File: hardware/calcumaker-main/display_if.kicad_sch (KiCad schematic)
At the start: 10 parts, among them J3 TO DISPLAY, U5 TPS61022RWUR, U6 74HCT125

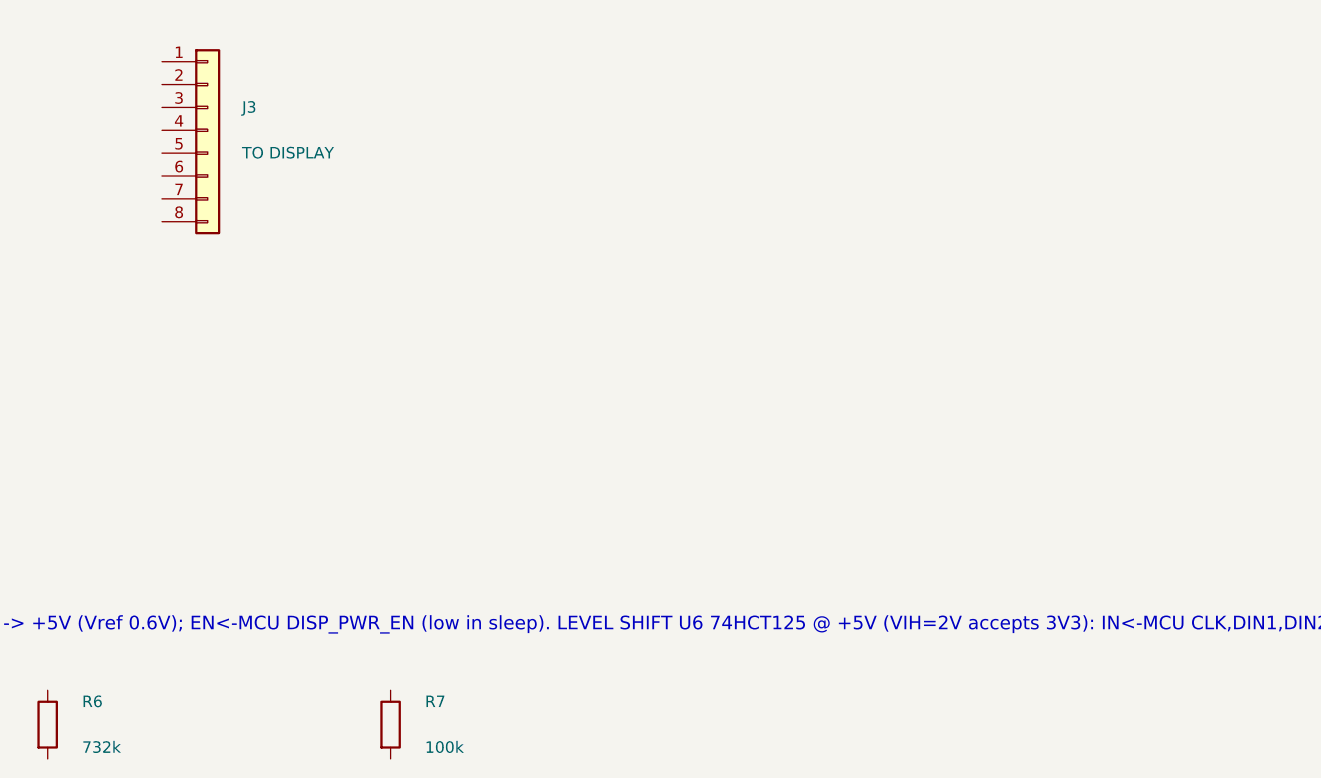
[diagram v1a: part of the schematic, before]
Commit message: Error handling: HP-style glass codes + DNP-optional aux OLED (display board)
Two layers, per design discussion:

ENGINE/APP — CalcError restructured: TypeError(&str) becomes Op(code, msg)
with class constructors at every site; code() gives the HP-16C-style glass
class (0 math domain, 1 register/flag, 2 bits/shift/word, 3 mode ranges,
4 too large, 5 no solution, 6 stack/entry, 7 dates, 8 statistics, 9 reserved
for crash recovery), text() the full string. App shows a transient 'Error N'
on the X row (cleared by the next key, like SHOW) and keeps the full text on
the status line — the duplicated error-string mapping in run_owned/flush is
now one report() helper. All of 'Error N' renders on the 7-seg. 211 tests.

HARDWARE — the aux OLED lands on the DISPLAY board (user decision): new
AuxDisplay sheet with J2, a 1x4 socket (PZ254V-11-04P C2691448) receiving a
standard 0.91in SSD1306 128x32 I2C module, DNP by default, hand-placed with
the THT digits. Interconnect grows 1x8 -> 1x10 (PZ254V-11-10P C492409, both
boards, pinout now ... 8=+3V3 9=SDA 10=SCL); I2C pull-ups R14/R15 4.7k on
the main board, DNP with the OLED. Both boards regenerate + check clean
(main 161, display 22 components). DESIGN.md documents the layered error
story and names the reusable 'DNP-optional aux' pattern; PARTS.md updated.

Co-Authored-By: Claude Fable 5 <noreply@anthropic.com>
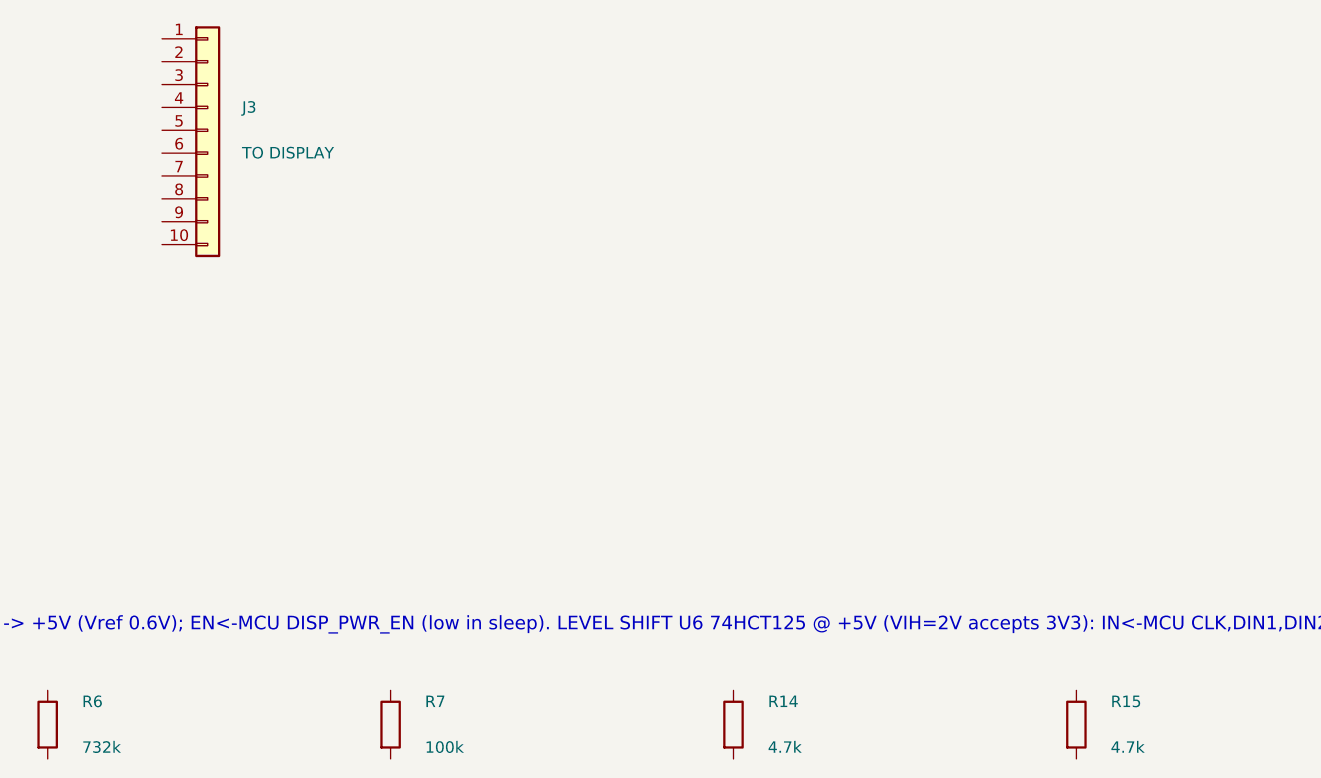
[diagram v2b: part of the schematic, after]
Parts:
- removed J3: TO DISPLAY, Connector_PinHeader_2.54mm:PinHeader_1x08_P2.54mm_Vertical, symbol Connector_Generic:Conn_01x08
- added J3: TO DISPLAY, Connector_PinHeader_2.54mm:PinHeader_1x10_P2.54mm_Vertical, symbol Connector_Generic:Conn_01x10
- added R14, R15: 4.7k, Resistor_SMD:R_0402_1005Metric, symbol Device:R
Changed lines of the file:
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@@
 		(instances
 			(project "calcumaker-main"
-				(path "/ca1c0000-0000-4000-8000-00000000ma01/354f9ce7-4ddf-44be-b9b3-f463ad410f0b"
+				(path "/ca1c0000-0000-4000-8000-00000000ma01/5a080947-7cc4-4e41-bc3c-27cf4b2ace01"
 					(reference "U5")
 					(unit 1)
@@
 		(instances
 			(project "calcumaker-main"
-				(path "/ca1c0000-0000-4000-8000-00000000ma01/354f9ce7-4ddf-44be-b9b3-f463ad410f0b"
+				(path "/ca1c0000-0000-4000-8000-00000000ma01/5a080947-7cc4-4e41-bc3c-27cf4b2ace01"
 					(reference "U6")
 					(unit 1)
@@
 	)
 	(symbol
-		(lib_id "Connector_Generic:Conn_01x08")
+		(lib_id "Connector_Generic:Conn_01x10")
 		(at 238.7600 55.8800 0)
 		(unit 1)
@@
 			(effects (font (size 1.27 1.27)) (justify left))
 		)
-		(property "Footprint" "Connector_PinHeader_2.54mm:PinHeader_1x08_P2.54mm_Vertical"
+		(property "Footprint" "Connector_PinHeader_2.54mm:PinHeader_1x10_P2.54mm_Vertical"
 			(at 238.7600 55.8800 0)
 			(effects (font (size 1.27 1.27))) (hide yes)
@@
 			(effects (font (size 1.27 1.27))) (hide yes)
 		)
-		(property "LCSC" "C492407"
+		(property "LCSC" "C492409"
 			(at 238.7600 55.8800 0)
 			(effects (font (size 1.27 1.27))) (hide yes)
 		)
-		(property "MPN" "PZ254V-11-08P"
+		(property "MPN" "PZ254V-11-10P"
 			(at 238.7600 55.8800 0)
 			(effects (font (size 1.27 1.27))) (hide yes)
@@
 		(pin "7")
 		(pin "8")
-		(instances
-			(project "calcumaker-main"
-				(path "/ca1c0000-0000-4000-8000-00000000ma01/354f9ce7-4ddf-44be-b9b3-f463ad410f0b"
+		(pin "9")
+		(pin "10")
+		(instances
+			(project "calcumaker-main"
+				(path "/ca1c0000-0000-4000-8000-00000000ma01/5a080947-7cc4-4e41-bc3c-27cf4b2ace01"
 					(reference "J3")
 					(unit 1)
@@
 		(instances
 			(project "calcumaker-main"
-				(path "/ca1c0000-0000-4000-8000-00000000ma01/354f9ce7-4ddf-44be-b9b3-f463ad410f0b"
+				(path "/ca1c0000-0000-4000-8000-00000000ma01/5a080947-7cc4-4e41-bc3c-27cf4b2ace01"
 					(reference "L2")
 					(unit 1)
@@
 		(instances
 			(project "calcumaker-main"
-				(path "/ca1c0000-0000-4000-8000-00000000ma01/354f9ce7-4ddf-44be-b9b3-f463ad410f0b"
+				(path "/ca1c0000-0000-4000-8000-00000000ma01/5a080947-7cc4-4e41-bc3c-27cf4b2ace01"
 					(reference "C8")
 					(unit 1)
@@
 		(instances
 			(project "calcumaker-main"
-				(path "/ca1c0000-0000-4000-8000-00000000ma01/354f9ce7-4ddf-44be-b9b3-f463ad410f0b"
+				(path "/ca1c0000-0000-4000-8000-00000000ma01/5a080947-7cc4-4e41-bc3c-27cf4b2ace01"
 					(reference "C9")
 					(unit 1)
@@
 		(instances
 			(project "calcumaker-main"
-				(path "/ca1c0000-0000-4000-8000-00000000ma01/354f9ce7-4ddf-44be-b9b3-f463ad410f0b"
+				(path "/ca1c0000-0000-4000-8000-00000000ma01/5a080947-7cc4-4e41-bc3c-27cf4b2ace01"
 					(reference "C10")
 					(unit 1)
@@
 		(instances
 			(project "calcumaker-main"
-				(path "/ca1c0000-0000-4000-8000-00000000ma01/354f9ce7-4ddf-44be-b9b3-f463ad410f0b"
+				(path "/ca1c0000-0000-4000-8000-00000000ma01/5a080947-7cc4-4e41-bc3c-27cf4b2ace01"
 					(reference "C11")
 					(unit 1)
@@
 		(instances
 			(project "calcumaker-main"
-				(path "/ca1c0000-0000-4000-8000-00000000ma01/354f9ce7-4ddf-44be-b9b3-f463ad410f0b"
+				(path "/ca1c0000-0000-4000-8000-00000000ma01/5a080947-7cc4-4e41-bc3c-27cf4b2ace01"
 					(reference "R6")
 					(unit 1)
@@
 		(instances
 			(project "calcumaker-main"
-				(path "/ca1c0000-0000-4000-8000-00000000ma01/354f9ce7-4ddf-44be-b9b3-f463ad410f0b"
+				(path "/ca1c0000-0000-4000-8000-00000000ma01/5a080947-7cc4-4e41-bc3c-27cf4b2ace01"
 					(reference "R7")
 					(unit 1)
 				)
+			)
+		)
+	)
+	(symbol
+		(lib_id "Device:R")
+		(at 297.1800 121.9200 0)
+		(unit 1)
+		(exclude_from_sim no)
+		(in_bom yes)
+		(on_board yes)
+		(dnp no)
+		(property "Reference" "R14"
+			(at 300.9900 119.3800 0)
+			(effects (font (size 1.27 1.27)) (justify left))
+		)
+		(property "Value" "4.7k"
+			(at 300.9900 124.4600 0)
+			(effects (font (size 1.27 1.27)) (justify left))
+		)
+		(property "Footprint" "Resistor_SMD:R_0402_1005Metric"
+			(at 297.1800 121.9200 0)
+			(effects (font (size 1.27 1.27))) (hide yes)
+		)
+		(property "Datasheet" "~"
+			(at 297.1800 121.9200 0)
+			(effects (font (size 1.27 1.27))) (hide yes)
+		)
+		(property "LCSC" "C25900"
+			(at 297.1800 121.9200 0)
+			(effects (font (size 1.27 1.27))) (hide yes)
+		)
+		(pin "1")
+		(pin "2")
+		(instances
+			(project "calcumaker-main"
+				(path "/ca1c0000-0000-4000-8000-00000000ma01/5a080947-7cc4-4e41-bc3c-27cf4b2ace01"
+					(reference "R14")
+					(unit 1)
+				)
+			)
+		)
+	)
+	(symbol
+		(lib_id "Device:R")
+		(at 335.2800 121.9200 0)
+		(unit 1)
+		(exclude_from_sim no)
+		(in_bom yes)
+		(on_board yes)
+		(dnp no)
+		(property "Reference" "R15"
+			(at 339.0900 119.3800 0)
+			(effects (font (size 1.27 1.27)) (justify left))
+		)
+		(property "Value" "4.7k"
+			(at 339.0900 124.4600 0)
+			(effects (font (size 1.27 1.27)) (justify left))
+		)
+		(property "Footprint" "Resistor_SMD:R_0402_1005Metric"
+			(at 335.2800 121.9200 0)
+			(effects (font (size 1.27 1.27))) (hide yes)
+		)
+		(property "Datasheet" "~"
+			(at 335.2800 121.9200 0)
+			(effects (font (size 1.27 1.27))) (hide yes)
+		)
+		(property "LCSC" "C25900"
+			(at 335.2800 121.9200 0)
+			(effects (font (size 1.27 1.27))) (hide yes)
+		)
+		(pin "1")
+		(pin "2")
+		(instances
+			(project "calcumaker-main"
+				(path "/ca1c0000-0000-4000-8000-00000000ma01/5a080947-7cc4-4e41-bc3c-27cf4b2ace01"
+					(reference "R15")
+					(unit 1)
+				)
